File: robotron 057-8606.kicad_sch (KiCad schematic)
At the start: 6 parts, among them J5 Conn_02x13_Odd_Even, U10 74LS123, X1 EFS29, X2 EFS13 Interleaved, X3 EFS13, X4 Conn_02x30_Top_Bottom

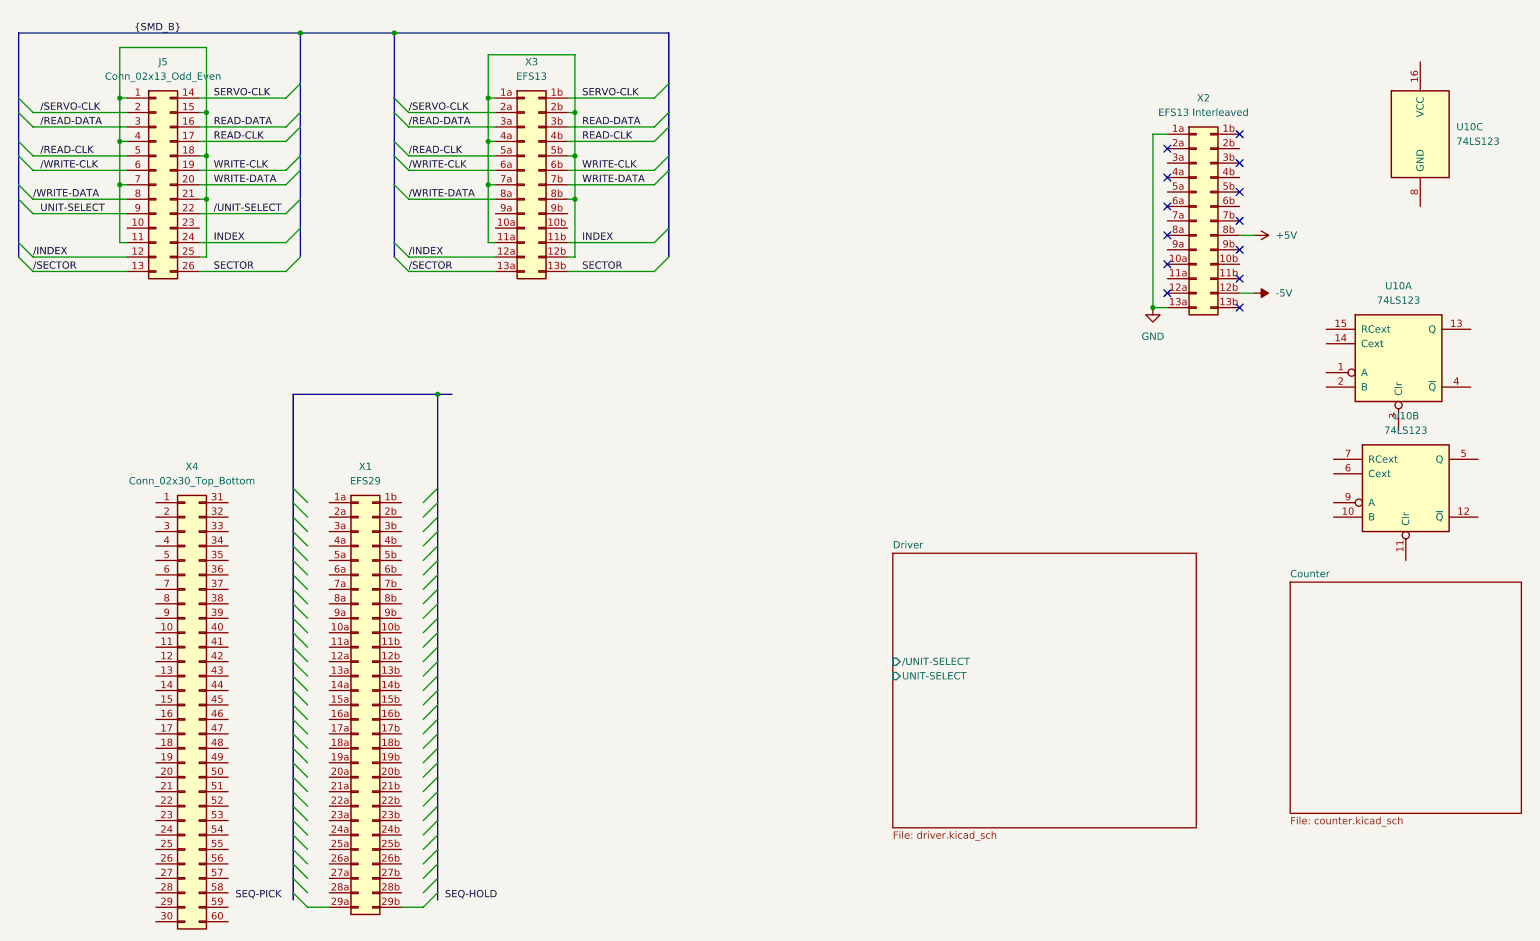
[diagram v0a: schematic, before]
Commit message: Einige Verbindungen im Bereich des Zählers ermittelt
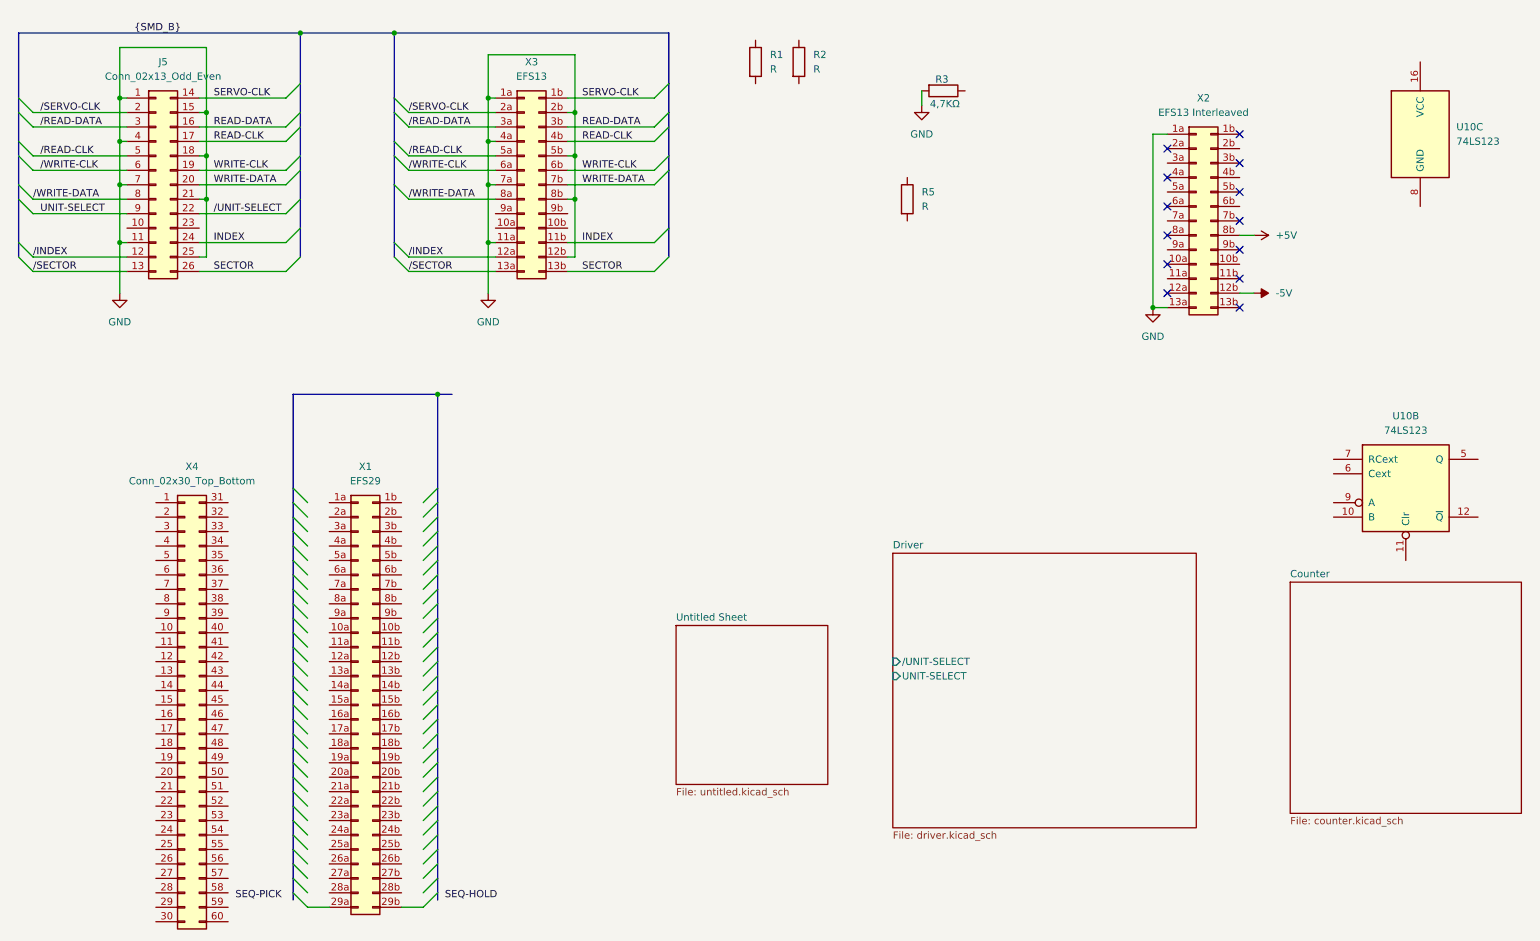
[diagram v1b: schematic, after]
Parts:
- removed unit 1 of U10
- added R1, R2, R5: R, Resistor_THT:R_Axial_DIN0207_L6.3mm_D2.5mm_P7.62mm_Horizontal, symbol Device:R
- added R3: 4,7KΩ, Resistor_THT:R_Axial_DIN0207_L6.3mm_D2.5mm_P7.62mm_Horizontal, symbol Device:R
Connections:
- net GND: now also J5.1 (Pin_1), J5.11 (Pin_11), J5.15 (Pin_15), J5.18 (Pin_18), J5.21 (Pin_21), J5.25 (Pin_25), J5.4 (Pin_4), J5.7 (Pin_7), X3.11a (Pin_11a), X3.12b (Pin_12b), X3.1a (Pin_1a), X3.2b (Pin_2b), X3.4a (Pin_4a), X3.5b (Pin_5b), X3.7a (Pin_7a), X3.8b (Pin_8b), R3.2
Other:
- added sheet Untitled Sheet (untitled.kicad_sch)

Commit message: Aufnahme Schaltplan wip
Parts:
- added C1, C10, C11, C12, C13, C14, C15, C16, C17, C2, C3, C4, C5, C6, C7, C8, C9: C_Small, symbol Device:C_Small
- added R11, R7, R8: R, Resistor_THT:R_Axial_DIN0207_L6.3mm_D2.5mm_P7.62mm_Horizontal, symbol Device:R
- R1: value R -> 470Ω
- R2: value R -> 22Ω
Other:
- removed sheet Untitled Sheet
- sheet Driver ports: added SRV_CLK, SRV_CLK_TTL, /SRV_CLK; removed none
- moved on the sheet: R1, R2, R3, R5, U10B, U10C, X2

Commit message: rev eng wip
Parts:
- removed unit 2 of U10
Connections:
- net Counter/MonoflopA: now reaches X2.6b (Pin_6b)
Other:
- sheet Counter ports: added CLK_UP, LOAD_TTL______, MonoflopA, SRV_CLK_TTL, U5_QA, UNIT_SELECT_TTL; removed none
- sheet Driver ports: added LOAD_TTL___, U5_QA, UNIT_SELECT_TTL; removed none
- moved on the sheet: R1, R2, R3

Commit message: Busses Names and more
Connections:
- net TAG1: now reaches X4.1 (Pin_1)
- net Bit6: now reaches X4.10 (Pin_10)
- net Bit7: now reaches X4.11 (Pin_11)
- net Bit8: now reaches X4.12 (Pin_12)
- net Bit9: now reaches X4.13 (Pin_13)
- net Open-Cable-Detect: now reaches X4.14 (Pin_14)
- net Fault: now reaches X4.15 (Pin_15)
- net Seek-Error: now reaches X4.16 (Pin_16)
- net On-Cylinder: now reaches X4.17 (Pin_17)
- net Index: now reaches X4.18 (Pin_18)
- net Unit-Ready: now reaches X4.19 (Pin_19)
- net TAG2: now reaches X4.2 (Pin_2)
- net Address-Mark-Found: now reaches X4.20 (Pin_20)
- net Busy: now reaches X4.21 (Pin_21)
- net Unit-Select-Tag: now reaches X4.22 (Pin_22)
- net Unit-Select-Bit0: now reaches X4.23 (Pin_23)
- net Unit-Select-Bit1: now reaches X4.24 (Pin_24)
- net Sector: now reaches X4.25 (Pin_25)
- net Unit-Select-Bit2: now reaches X4.26 (Pin_26)
- net Unit-Select-Bit3: now reaches X4.27 (Pin_27)
- net Write-Protected: now reaches X4.28 (Pin_28)
- net Power-Sequence-Hold: now reaches X4.29 (Pin_29)
- net TAG3: now reaches X4.3 (Pin_3)
- net Bit10: now reaches X4.30 (Pin_30)
- net /Tag1: now reaches X4.31 (Pin_31)
- net /Tag2: now reaches X4.32 (Pin_32)
- net /Tag3: now reaches X4.33 (Pin_33)
- net /Bit0: now reaches X4.34 (Pin_34)
- net /Bit1: now reaches X4.35 (Pin_35)
- net /Bit2: now reaches X4.36 (Pin_36)
- net /Bit3: now reaches X4.37 (Pin_37)
- net /Bit4: now reaches X4.38 (Pin_38)
- net /Bit5: now reaches X4.39 (Pin_39)
- net Bit0: now reaches X4.4 (Pin_4)
- net /Bit6: now reaches X4.40 (Pin_40)
- net /Bit7: now reaches X4.41 (Pin_41)
- net /Bit8: now reaches X4.42 (Pin_42)
- net /Bit9: now reaches X4.43 (Pin_43)
- net /Open-Cable-Detect: now reaches X4.44 (Pin_44)
- net /Fault: now reaches X4.45 (Pin_45)
- net /Seek-Error: now reaches X4.46 (Pin_46)
- net /On-Cylinder: now reaches X4.47 (Pin_47)
- net /Index: now reaches X4.48 (Pin_48)
- net /Unit-Ready: now reaches X4.49 (Pin_49)
- net Bit1: now reaches X4.5 (Pin_5)
- net /Address-Mark-Found: now reaches X4.50 (Pin_50)
- net /Busy: now reaches X4.51 (Pin_51)
- net /Unit-Select-Tag: now reaches X4.52 (Pin_52)
- net /Unit-Select-Bit0: now reaches X4.53 (Pin_53)
- net /Unit-Select-Bit1: now reaches X4.54 (Pin_54)
- net /Sector: now reaches X4.55 (Pin_55)
- net /Unit-Select-Bit2: now reaches X4.56 (Pin_56)
- net /Unit-Select-Bit3: now reaches X4.57 (Pin_57)
- net /Write-Protected: now reaches X4.58 (Pin_58)
- net Power-Sequence-Pick: now reaches X4.59 (Pin_59)
- net Bit2: now reaches X4.6 (Pin_6)
- net /Bit10: now reaches X4.60 (Pin_60)
- net Bit3: now reaches X4.7 (Pin_7)
- net Bit4: now reaches X4.8 (Pin_8)
- net Bit5: now reaches X4.9 (Pin_9)
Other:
- sheet Counter ports: added BIT10_TTL; removed U5_QA
- sheet Driver ports: added BIT10_TTL; removed U5_QA

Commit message: weitere verdrahtungen nachvollzogen
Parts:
- removed C8, C9: C_Small, symbol Device:C_Small
- added R12, R13, R14, R15, R16, R17, R18, R19, R20, R21, R24, R25, R26, R27, R28, R29, R30, R31, R32: R, Resistor_THT:R_Axial_DIN0207_L6.3mm_D2.5mm_P7.62mm_Horizontal, symbol Device:R
- C1, C10, C11, C12, C13, C14, C15, C16, C17, C2, C3, C4, C5, C6, C7: footprint (none) -> Capacitor_THT:C_Disc_D3.0mm_W1.6mm_P2.50mm
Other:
- moved on the sheet: X1
